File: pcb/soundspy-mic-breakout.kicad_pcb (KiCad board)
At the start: 2 copper layers, 15 x 12 mm, 4 parts, among them J1 ESP32, U1 ICS-43434

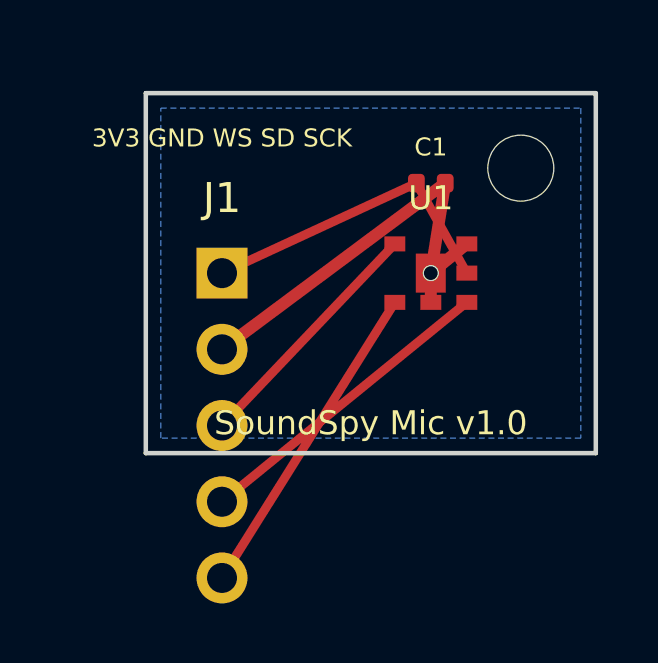
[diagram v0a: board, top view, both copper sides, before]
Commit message: PCB: node carrier board + fix breakout layout
soundspy-node.kicad_pcb:
- ESP32 38-pin DevKit carrier (30x68mm)
- ICS-43434 on standoff pins, sound port hole at top
- USB-C notch at bottom edge for case passthrough
- 4x M2 mounting holes
- 100nF decoupling cap, GND fill on B.Cu
- I2S traces (SCK/WS/SD) routed non-crossing

soundspy-mic-breakout.kicad_pcb (v1.1):
- Fix: J1 was off-board (pads at y=16mm on 12mm board)
- Center J1 vertically, all pads within bounds
- Fix crossing traces, correct pad-to-net assignments
- Use standard KiCad footprint libraries

Preview PNGs added for both boards
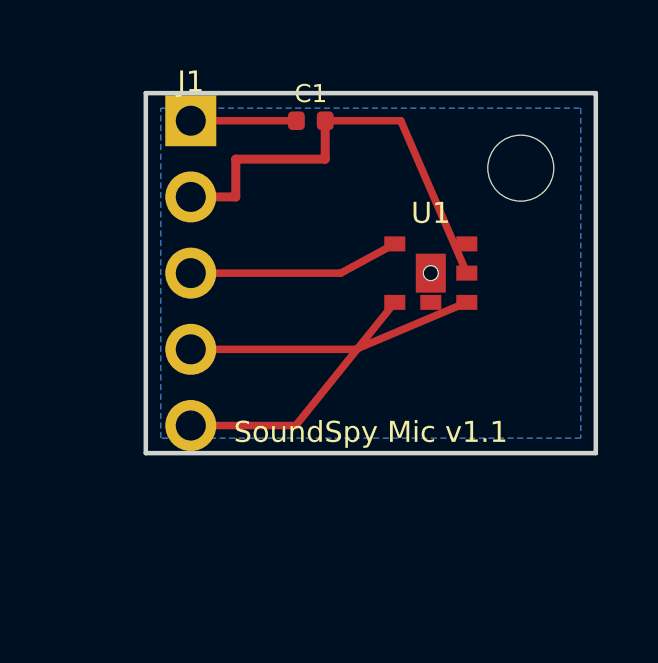
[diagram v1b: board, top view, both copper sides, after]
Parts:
- added ?: , at,  at (0.00, 0.00)
- U1: footprint soundspy:ICS-43434 -> Package_LGA:LGA-8_3.5x2.65mm_P1.27mm
- moved J1 5.19 mm to (1.50, 0.92)
- moved C1 4.51 mm to (5.50, 0.92)
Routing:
- net GND: track 14.8 -> 7.02 mm
- net I2S_SCK: track 10.8 -> 8.77 mm
- net I2S_WS: track 8.36 -> 7.05 mm
- net I2S_SD: track 10.5 -> 9.52 mm
- net 3V3: track 10.6 -> 11.6 mm
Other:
- board text added: "SoundSpy Mic v1.1"
- board text removed: "3V3 GND WS SD SCK"
- board text removed: "SoundSpy Mic v1.0"
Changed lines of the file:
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@@
     (title "SoundSpy Mic Breakout")
     (date "2026-07-30")
-    (rev "1.0")
-    (comment 1 "ICS-43434 breakout adapter for ESP32 DevKit")
+    (rev "1.1")
+    (comment 1 "ICS-43434 I2S mic breakout for ESP32")
   )
   (layers
@@
   (gr_line (start 15 12) (end 0 12) (layer "Edge.Cuts") (width 0.15))
   (gr_line (start 0 12) (end 0 0) (layer "Edge.Cuts") (width 0.15))
+  ;; J1 centered vertically: pin1(3V3) at y=0.92, pin5(SCK) at y=11.08
+  (footprint "Connector_PinHeader_2.54mm:PinHeader_1x05_P2.54mm_Vertical" (at 1.5 0.92 0) (layer "F.Cu")
+    (fp_text reference "J1" (at 0 -1.3) (layer "F.SilkS") (effects (font (size 0.7 0.7) (thickness 0.1))))
+    (fp_text value "ESP32" (at 3.0 5.08) (layer "F.Fab") (effects (font (size 0.7 0.7) (thickness 0.1))))
+    (pad "1" thru_hole rect   (at 0 0)     (size 1.7 1.7) (drill 1.0) (layers "*.Cu" "*.Mask") (net 1 "3V3"))
+    (pad "2" thru_hole circle (at 0 2.54)  (size 1.7 1.7) (drill 1.0) (layers "*.Cu" "*.Mask") (net 2 "GND"))
+    (pad "3" thru_hole circle (at 0 5.08)  (size 1.7 1.7) (drill 1.0) (layers "*.Cu" "*.Mask") (net 3 "I2S_WS"))
+    (pad "4" thru_hole circle (at 0 7.62)  (size 1.7 1.7) (drill 1.0) (layers "*.Cu" "*.Mask") (net 4 "I2S_SD"))
+    (pad "5" thru_hole circle (at 0 10.16) (size 1.7 1.7) (drill 1.0) (layers "*.Cu" "*.Mask") (net 5 "I2S_SCK"))
+  )
+  ;; Absolute J1 pad positions (footprint at y=0.92):
+  ;;   pin1 3V3:    (1.5, 0.92)
+  ;;   pin2 GND:    (1.5, 3.46)
+  ;;   pin3 I2S_WS: (1.5, 6.00)
+  ;;   pin4 I2S_SD: (1.5, 8.54)
+  ;;   pin5 I2S_SCK:(1.5, 11.08)
+  ;; U1 - ICS-43434 LGA, placed at (9.5, 6.0)
+  ;; Absolute pad positions:
+  ;;   pin1 WS:  (8.3,  5.025)
+  ;;   pin2 SCK: (8.3,  6.975)
+  ;;   pin3 GND: (9.5,  6.975)
+  ;;   pin4 GND: (10.7, 5.025)
+  ;;   pin5 VDD: (10.7, 6.0)
+  ;;   pin6 SD:  (10.7, 6.975)
+  ;;   pin7 EP:  (9.5,  6.0)
+  (footprint "Package_LGA:LGA-8_3.5x2.65mm_P1.27mm" (at 9.5 6.0 0) (layer "F.Cu")
+    (fp_text reference "U1" (at 0 -2.0) (layer "F.SilkS") (effects (font (size 0.7 0.7) (thickness 0.1))))
+    (fp_text value "ICS-43434" (at 0 2.0) (layer "F.Fab") (effects (font (size 0.7 0.7) (thickness 0.1))))
+    (pad "1" smd rect (at -1.2 -0.975) (size 0.7 0.5) (layers "F.Cu" "F.Mask" "F.Paste") (net 3 "I2S_WS"))
+    (pad "2" smd rect (at -1.2  0.975) (size 0.7 0.5) (layers "F.Cu" "F.Mask" "F.Paste") (net 5 "I2S_SCK"))
+    (pad "3" smd rect (at  0    0.975) (size 0.7 0.5) (layers "F.Cu" "F.Mask" "F.Paste") (net 2 "GND"))
+    (pad "4" smd rect (at  1.2 -0.975) (size 0.7 0.5) (layers "F.Cu" "F.Mask" "F.Paste") (net 2 "GND"))
+    (pad "5" smd rect (at  1.2  0)     (size 0.7 0.5) (layers "F.Cu" "F.Mask" "F.Paste") (net 1 "3V3"))
+    (pad "6" smd rect (at  1.2  0.975) (size 0.7 0.5) (layers "F.Cu" "F.Mask" "F.Paste") (net 4 "I2S_SD"))
+    (pad "7" smd rect (at  0    0)     (size 1.0 1.3) (layers "F.Cu" "F.Mask" "F.Paste") (net 2 "GND"))
+    (pad "" np_thru_hole circle (at 0 0) (size 0.5 0.5) (drill 0.5) (layers "*.Cu" "*.Mask"))
+  )
+  ;; C1 - 100nF 0402 at (5.5, 0.92) - near 3V3/GND pins
+  ;; pad1 (3V3) abs: (5.02, 0.92)
+  ;; pad2 (GND) abs: (5.98, 0.92)
+  (footprint "Capacitor_SMD:C_0402_1005Metric" (at 5.5 0.92 0) (layer "F.Cu")
+    (fp_text reference "C1" (at 0 -0.9) (layer "F.SilkS") (effects (font (size 0.6 0.6) (thickness 0.1))))
+    (fp_text value "100nF" (at 0 0.9) (layer "F.Fab") (effects (font (size 0.6 0.6) (thickness 0.1))))
+    (pad "1" smd roundrect (at -0.48 0) (size 0.56 0.62) (layers "F.Cu" "F.Mask" "F.Paste") (roundrect_rratio 0.25) (net 1 "3V3"))
+    (pad "2" smd roundrect (at  0.48 0) (size 0.56 0.62) (layers "F.Cu" "F.Mask" "F.Paste") (roundrect_rratio 0.25) (net 2 "GND"))
+  )
+  ;; Mounting hole M2 at (12.5, 2.5) - top right, safely inside board
   (footprint "MountingHole:MountingHole_2.2mm_M2" (at 12.5 2.5) (layer "F.Cu")
     (pad "" np_thru_hole circle (at 0 0) (size 2.2 2.2) (drill 2.2) (layers "*.Cu" "*.Mask"))
   )
-  (footprint "Connector_PinHeader_2.54mm:PinHeader_1x05_P2.54mm_Vertical" (at 2.54 6.0 0) (layer "F.Cu")
-    (fp_text reference "J1" (at 0 -2.5) (layer "F.SilkS") (effects (font (size 1 1) (thickness 0.15))))
-    (fp_text value "ESP32" (at 0 12.7) (layer "F.Fab") (effects (font (size 1 1) (thickness 0.15))))
-    (pad "1" thru_hole rect (at 0 0) (size 1.7 1.7) (drill 1.0) (layers "*.Cu" "*.Mask") (net 1 "3V3"))
-    (pad "2" thru_hole circle (at 0 2.54) (size 1.7 1.7) (drill 1.0) (layers "*.Cu" "*.Mask") (net 2 "GND"))
-    (pad "3" thru_hole circle (at 0 5.08) (size 1.7 1.7) (drill 1.0) (layers "*.Cu" "*.Mask") (net 3 "I2S_WS"))
-    (pad "4" thru_hole circle (at 0 7.62) (size 1.7 1.7) (drill 1.0) (layers "*.Cu" "*.Mask") (net 4 "I2S_SD"))
-    (pad "5" thru_hole circle (at 0 10.16) (size 1.7 1.7) (drill 1.0) (layers "*.Cu" "*.Mask") (net 5 "I2S_SCK"))
+  ;; ── Traces ────────────────────────────────────────────────────────────────────
+  ;; All routes verified non-crossing by going through distinct Y corridors:
+  ;;   3V3  : top corridor  Y~0.92
+  ;;   GND  : Y~2.0 jog then via B.Cu pour
+  ;;   WS   : Y~6.0
+  ;;   SD   : Y~8.54
+  ;;   SCK  : Y~11.08 then diagonal up to U1
+  ;; 3V3: J1.1(1.5,0.92) -> C1.1(5.02,0.92) -> U1.5(10.7,6.0)
+  (segment (start 1.5  0.92) (end 5.02 0.92) (width 0.25) (layer "F.Cu") (net 1))
+  (segment (start 5.98 0.92) (end 8.5  0.92) (width 0.25) (layer "F.Cu") (net 1))
+  (segment (start 8.5  0.92) (end 10.7 6.0)  (width 0.25) (layer "F.Cu") (net 1))
+  ;; GND: J1.2(1.5,3.46) -> C1.2(5.98,0.92) jog through Y=2.2
+  (segment (start 1.5  3.46) (end 3.0  3.46) (width 0.3)  (layer "F.Cu") (net 2))
+  (segment (start 3.0  3.46) (end 3.0  2.2)  (width 0.3)  (layer "F.Cu") (net 2))
+  (segment (start 3.0  2.2)  (end 5.98 2.2)  (width 0.3)  (layer "F.Cu") (net 2))
+  (segment (start 5.98 2.2)  (end 5.98 0.92) (width 0.3)  (layer "F.Cu") (net 2))
+  ;; GND also connects to U1 EP via B.Cu zone (no explicit trace needed)
+  ;; WS: J1.3(1.5,6.0) -> U1.1(8.3,5.025) -- straight horizontal then short diagonal
+  (segment (start 1.5  6.0)  (end 6.5  6.0)  (width 0.25) (layer "F.Cu") (net 3))
+  (segment (start 6.5  6.0)  (end 8.3  5.025)(width 0.25) (layer "F.Cu") (net 3))
+  ;; SD: J1.4(1.5,8.54) -> U1.6(10.7,6.975) -- route below U1
+  (segment (start 1.5  8.54) (end 7.0  8.54) (width 0.25) (layer "F.Cu") (net 4))
+  (segment (start 7.0  8.54) (end 10.7 6.975)(width 0.25) (layer "F.Cu") (net 4))
+  ;; SCK: J1.5(1.5,11.08) -> U1.2(8.3,6.975) -- route along bottom then angle up
+  (segment (start 1.5  11.08) (end 5.0  11.08) (width 0.25) (layer "F.Cu") (net 5))
+  (segment (start 5.0  11.08) (end 8.3   6.975) (width 0.25) (layer "F.Cu") (net 5))
+  ;; ── Silkscreen ────────────────────────────────────────────────────────────────
+  (gr_text "SoundSpy Mic v1.1" (at 7.5 11.3) (layer "F.SilkS")
+    (effects (font (size 0.7 0.7) (thickness 0.1)))
   )
-  (footprint "soundspy:ICS-43434" (at 9.5 6.0 0) (layer "F.Cu")
-    (fp_text reference "U1" (at 0 -2.5) (layer "F.SilkS") (effects (font (size 0.8 0.8) (thickness 0.12))))
-    (fp_text value "ICS-43434" (at 0 3.5) (layer "F.Fab") (effects (font (size 0.8 0.8) (thickness 0.12))))
-    (pad "1" smd rect (at -1.2 -0.975) (size 0.7 0.5) (layers "F.Cu" "F.Mask" "F.Paste") (net 3 "I2S_WS"))
-    (pad "2" smd rect (at -1.2 0.975) (size 0.7 0.5) (layers "F.Cu" "F.Mask" "F.Paste") (net 5 "I2S_SCK"))
-    (pad "3" smd rect (at 0 0.975) (size 0.7 0.5) (layers "F.Cu" "F.Mask" "F.Paste") (net 2 "GND"))
-    (pad "4" smd rect (at 1.2 -0.975) (size 0.7 0.5) (layers "F.Cu" "F.Mask" "F.Paste") (net 2 "GND"))
-    (pad "5" smd rect (at 1.2 0) (size 0.7 0.5) (layers "F.Cu" "F.Mask" "F.Paste") (net 1 "3V3"))
-    (pad "6" smd rect (at 1.2 0.975) (size 0.7 0.5) (layers "F.Cu" "F.Mask" "F.Paste") (net 4 "I2S_SD"))
-    (pad "7" smd rect (at 0 0) (size 1.0 1.3) (layers "F.Cu" "F.Mask" "F.Paste") (net 2 "GND"))
-    (pad "" np_thru_hole circle (at 0 0) (size 0.5 0.5) (drill 0.5) (layers "*.Cu" "*.Mask"))
-  )
-  (footprint "Capacitor_SMD:C_0402_1005Metric" (at 9.5 3.0 0) (layer "F.Cu")
-    (fp_text reference "C1" (at 0 -1.2) (layer "F.SilkS") (effects (font (size 0.6 0.6) (thickness 0.1))))
-    (fp_text value "100nF" (at 0 1.2) (layer "F.Fab") (effects (font (size 0.6 0.6) (thickness 0.1))))
-    (pad "1" smd roundrect (at -0.48 0) (size 0.56 0.62) (layers "F.Cu" "F.Mask" "F.Paste") (roundrect_rratio 0.25) (net 1 "3V3"))
-    (pad "2" smd roundrect (at 0.48 0) (size 0.56 0.62) (layers "F.Cu" "F.Mask" "F.Paste") (roundrect_rratio 0.25) (net 2 "GND"))
-  )
-  (segment (start 2.54 6.0) (end 9.02 3.0) (width 0.3) (layer "F.Cu") (net 1))
-  (segment (start 9.02 3.0) (end 10.7 6.0) (width 0.3) (layer "F.Cu") (net 1))
-  (segment (start 2.54 8.54) (end 9.98 3.0) (width 0.4) (layer "F.Cu") (net 2))
-  (segment (start 9.98 3.0) (end 9.5 6.0) (width 0.4) (layer "F.Cu") (net 2))
-  (segment (start 9.5 6.0) (end 9.5 6.975) (width 0.4) (layer "F.Cu") (net 2))
-  (segment (start 9.5 6.0) (end 10.7 5.025) (width 0.4) (layer "F.Cu") (net 2))
-  (segment (start 2.54 11.08) (end 8.3 5.025) (width 0.3) (layer "F.Cu") (net 3))
-  (segment (start 2.54 13.62) (end 10.7 6.975) (width 0.3) (layer "F.Cu") (net 4))
-  (segment (start 2.54 16.16) (end 8.3 6.975) (width 0.3) (layer "F.Cu") (net 5))
-  (gr_text "SoundSpy Mic v1.0" (at 7.5 11.0) (layer "F.SilkS")
-    (effects (font (size 0.8 0.8) (thickness 0.12)))
-  )
-  (gr_text "3V3 GND WS SD SCK" (at 2.54 1.5) (layer "F.SilkS")
-    (effects (font (size 0.6 0.6) (thickness 0.1)))
-  )
+  ;; ── GND fill (B.Cu) ───────────────────────────────────────────────────────────
   (zone (net 2) (net_name "GND") (layer "B.Cu")
     (hatch edge 0.5)
